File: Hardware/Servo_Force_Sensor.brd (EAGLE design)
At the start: 25.4 x 25.4 mm, 1 part

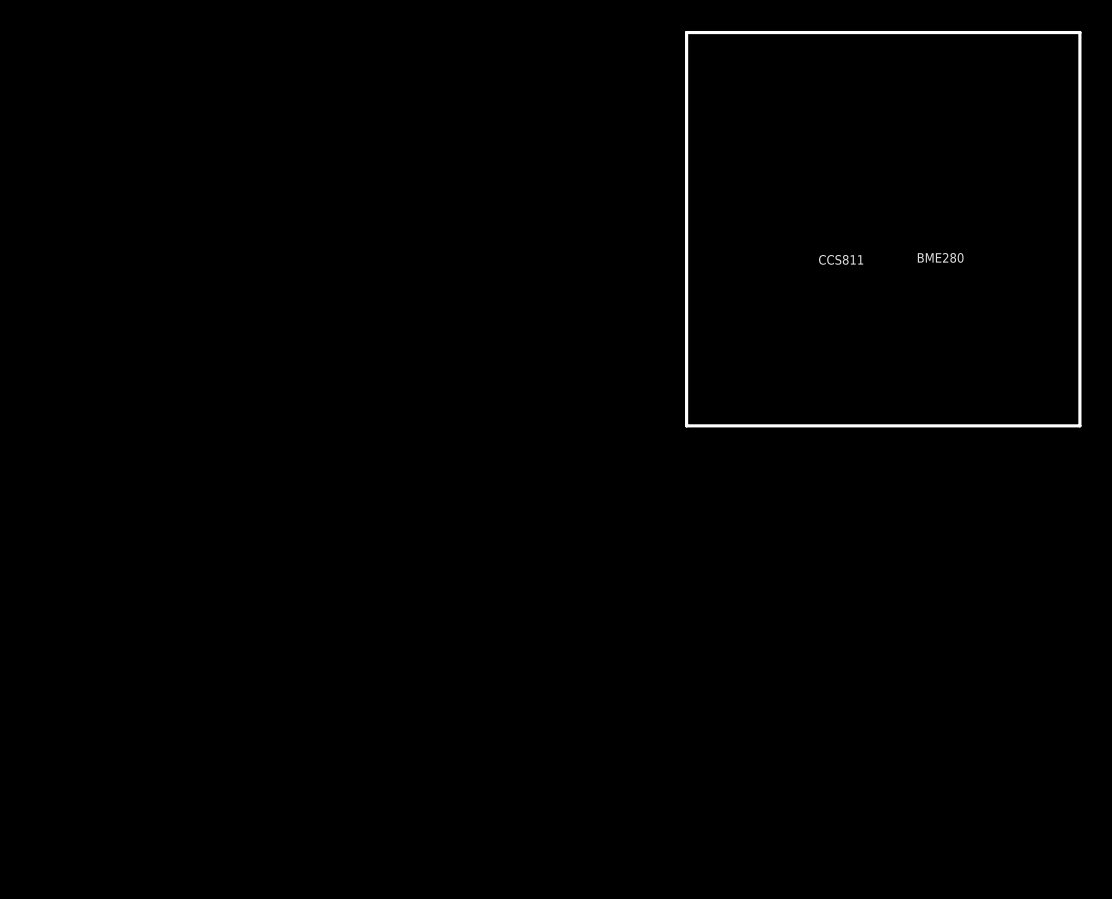
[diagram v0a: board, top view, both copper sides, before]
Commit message: library work for medium and large horns
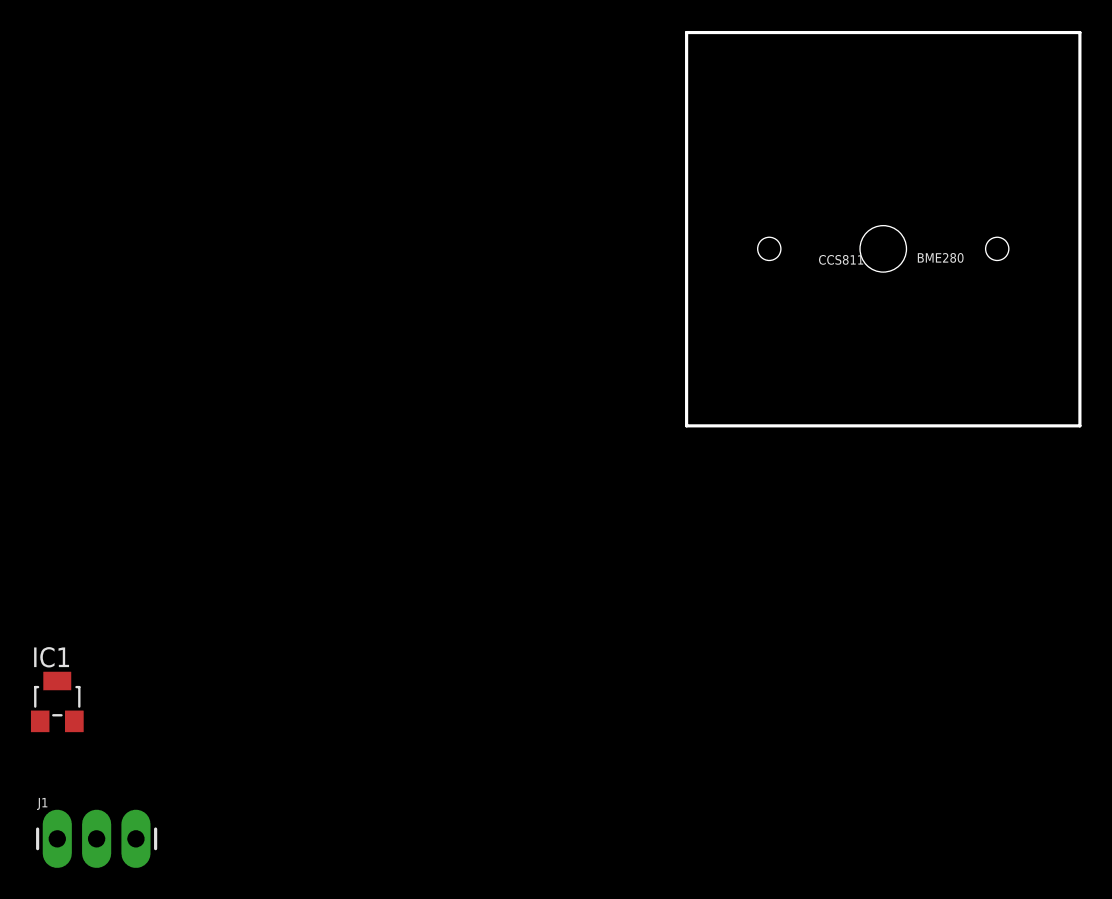
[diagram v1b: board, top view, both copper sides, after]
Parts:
- added IC1: A1302LH, allegro:SOT23-W
- added J1: (no value), SparkFun-Connectors:1X03_LONGPADS
- added U$1: (no value), Servo_Horns:MEDIUM_HORN_16MM
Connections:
- new net GND: IC1.3, J1.3
- new net OUT: IC1.2, J1.2
- new net VCC: IC1.1, J1.1
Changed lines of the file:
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@@
 <layer number="47" name="Measures" color="7" fill="1" visible="no" active="yes"/>
 <layer number="48" name="Document" color="7" fill="1" visible="no" active="yes"/>
-<layer number="49" name="Reference" color="7" fill="1" visible="no" active="yes"/>
+<layer number="49" name="Reference" color="13" fill="1" visible="yes" active="yes"/>
 <layer number="50" name="dxf" color="7" fill="1" visible="no" active="yes"/>
 <layer number="51" name="tDocu" color="6" fill="1" visible="yes" active="yes"/>
@@
 <layer number="115" name="ReferenceISLANDS" color="7" fill="1" visible="no" active="no"/>
 <layer number="116" name="Patch_BOT" color="9" fill="4" visible="no" active="no"/>
-<layer number="117" name="PM_Ref" color="26" fill="1" visible="yes" active="yes"/>
+<layer number="117" name="PM_Ref" color="26" fill="1" visible="no" active="yes"/>
 <layer number="118" name="Rect_Pads" color="7" fill="1" visible="no" active="no"/>
-<layer number="119" name="PF_Ref" color="31" fill="1" visible="yes" active="yes"/>
-<layer number="120" name="WFL_Ref" color="25" fill="1" visible="yes" active="yes"/>
+<layer number="119" name="PF_Ref" color="31" fill="1" visible="no" active="yes"/>
+<layer number="120" name="WFL_Ref" color="25" fill="1" visible="no" active="yes"/>
 <layer number="121" name="_tsilk" color="7" fill="1" visible="no" active="no"/>
 <layer number="122" name="_bsilk" color="7" fill="1" visible="no" active="no"/>
@@
 <attribute name="REV" value="" x="-13.97" y="-21.59" size="1.778" layer="27" display="off"/>
 </element>
+<element name="IC1" library="allegro" library_urn="urn:adsk.eagle:library:93" package="SOT23-W" package3d_urn="urn:adsk.eagle:package:3443/1" value="A1302LH" x="-40.64" y="-17.78" smashed="yes">
+<attribute name="MF" value="ALLEGRO MICROSYSTEMS, INC." x="-40.64" y="-17.78" size="1.778" layer="27" display="off"/>
+<attribute name="MPN" value="A1302ELHLT-T" x="-40.64" y="-17.78" size="1.778" layer="27" display="off"/>
+<attribute name="NAME" x="-42.29" y="-15.58" size="1.27" layer="25"/>
+<attribute name="OC_FARNELL" value="1457209" x="-40.64" y="-17.78" size="1.778" layer="27" display="off"/>
+<attribute name="OC_NEWARK" value="31K6638" x="-40.64" y="-17.78" size="1.778" layer="27" display="off"/>
+<attribute name="VALUE" x="-42.84" y="-21.63" size="1.27" layer="27"/>
+</element>
+<element name="J1" library="SparkFun-Connectors" package="1X03_LONGPADS" value="" x="-40.64" y="-26.67" smashed="yes">
+<attribute name="NAME" x="-41.91" y="-24.638" size="0.6096" layer="25" font="vector" ratio="20"/>
+<attribute name="VALUE" x="-41.91" y="-29.337" size="0.6096" layer="27" font="vector" ratio="20"/>
+</element>
+<element name="U$1" library="Servo_Horns" package="MEDIUM_HORN_16MM" value="" x="12.7" y="11.43" smashed="yes"/>
 </elements>
 <signals>
@@
 <vertex x="0" y="0"/>
 </polygon>
+<contactref element="IC1" pad="3"/>
+<contactref element="J1" pad="3"/>
+<wire x1="-40.64" y1="-16.48" x2="-35.56" y2="-26.67" width="0" layer="19" extent="1-1"/>
 </signal>
 <signal name="N$1">
+</signal>
+<signal name="VCC">
+<contactref element="IC1" pad="1"/>
+<contactref element="J1" pad="1"/>
+<wire x1="-41.74" y1="-19.08" x2="-40.64" y2="-26.67" width="0" layer="19" extent="1-1"/>
+</signal>
+<signal name="OUT">
+<contactref element="IC1" pad="2"/>
+<contactref element="J1" pad="2"/>
+<wire x1="-39.54" y1="-19.08" x2="-38.1" y2="-26.67" width="0" layer="19" extent="1-1"/>
 </signal>
 </signals>
@@
 </board>
 </drawing>
+<compatibility>
+<note version="8.2" severity="warning">
+Since Version 8.2, EAGLE supports online libraries. The ids
+of those online libraries will not be understood (or retained)
+with this version.
+</note>
+<note version="8.3" severity="warning">
+Since Version 8.3, EAGLE supports URNs for individual library
+assets (packages, symbols, and devices). The URNs of those assets
+will not be understood (or retained) with this version.
+</note>
+<note version="8.3" severity="warning">
+Since Version 8.3, EAGLE supports the association of 3D packages
+with devices in libraries, schematics, and board files. Those 3D
+packages will not be understood (or retained) with this version.
+</note>
+</compatibility>
 </eagle>

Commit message: finalized v01
outer shape done,
verified drill holes via lazer cut acrylic prototype
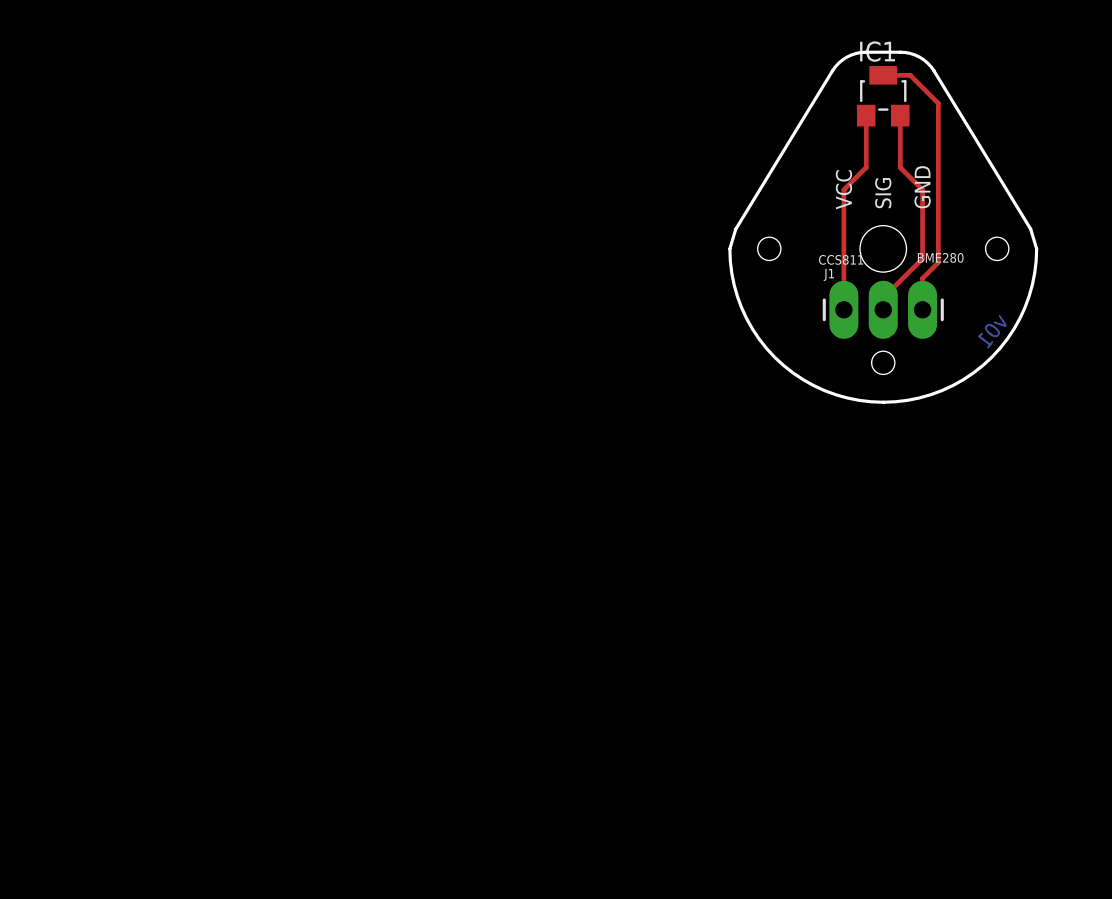
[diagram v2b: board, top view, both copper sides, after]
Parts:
- moved IC1 66.1 mm to (12.7, 21.3)
- moved J1 61.2 mm to (10.2, 7.49)
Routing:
- net GND: track 0.00 -> 18.1 mm
- net OUT: track 0.00 -> 14.2 mm
- net VCC: track 0.00 -> 13.1 mm
- removed copper zone on layer 1, net GND
- removed copper zone on layer 16, net GND
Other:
- board size 25.4 x 25.4 mm -> 19.8 x 22.6 mm
- board text added: "GND"
- board text added: "SIG"
- board text added: "VCC"
- board text added: "v01"
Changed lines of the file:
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@@
 <layer number="155" name="FabDoc3" color="7" fill="1" visible="no" active="no"/>
 <layer number="199" name="Contour" color="7" fill="1" visible="no" active="no"/>
-<layer number="200" name="200bmp" color="1" fill="10" visible="no" active="no"/>
+<layer number="200" name="200bmp" color="1" fill="10" visible="no" active="yes"/>
 <layer number="201" name="201bmp" color="2" fill="10" visible="no" active="no"/>
 <layer number="202" name="202bmp" color="3" fill="10" visible="no" active="no"/>
@@
 <board>
 <plain>
-<wire x1="0" y1="0" x2="0" y2="25.4" width="0.2032" layer="20"/>
-<wire x1="0" y1="25.4" x2="25.4" y2="25.4" width="0.2032" layer="20"/>
-<wire x1="25.4" y1="25.4" x2="25.4" y2="0" width="0.2032" layer="20"/>
-<wire x1="25.4" y1="0" x2="0" y2="0" width="0.2032" layer="20"/>
 <text x="16.51" y="-21.59" size="1.778" layer="51">Pete Lewis</text>
 <text x="8.509" y="10.414" size="0.6096" layer="25">CCS811</text>
@@
 <dimension x1="22.86" y1="22.86" x2="0" y2="22.86" x3="11.43" y3="30.48" textsize="1.778" layer="47"/>
 <text x="-1.27" y="-12.7" size="1.778" layer="47">Measurements in mm</text>
+<wire x1="22.225" y1="12.7" x2="15.982815625" y2="22.914484375" width="0.2032" layer="20"/>
+<wire x1="15.982815625" y1="22.914484375" x2="13.81548125" y2="24.13" width="0.2032" layer="20" curve="58.570451"/>
+<wire x1="13.81548125" y1="24.13" x2="11.58451875" y2="24.13" width="0.2032" layer="20"/>
+<wire x1="11.58451875" y1="24.13" x2="9.417184375" y2="22.914484375" width="0.2032" layer="20" curve="58.570391"/>
+<wire x1="9.417184375" y1="22.914484375" x2="3.175" y2="12.7" width="0.2032" layer="20"/>
+<wire x1="3.175" y1="12.7" x2="2.794" y2="11.43" width="0.2032" layer="20"/>
+<wire x1="22.606" y1="11.43" x2="22.225" y2="12.7" width="0.2032" layer="20"/>
+<text x="15.24" y="13.97" size="1.016" layer="21" font="vector" ratio="15" rot="R90" align="center-left">GND</text>
+<text x="10.16" y="13.97" size="1.016" layer="21" font="vector" ratio="15" rot="R90" align="center-left">VCC</text>
+<wire x1="2.794" y1="11.43" x2="12.7" y2="1.524" width="0.2032" layer="20" curve="90"/>
+<wire x1="12.7" y1="1.524" x2="22.606" y2="11.43" width="0.2032" layer="20" curve="90"/>
+<text x="12.7" y="13.97" size="1.016" layer="21" font="vector" ratio="15" rot="R90" align="center-left">SIG</text>
+<text x="19.016790625" y="5.208446875" size="1.016" layer="16" font="vector" ratio="20" rot="MR128" align="center-left">v01</text>
 </plain>
 <attributes>
@@
 <attribute name="REV" value="" x="-13.97" y="-21.59" size="1.778" layer="27" display="off"/>
 </element>
-<element name="IC1" library="allegro" library_urn="urn:adsk.eagle:library:93" package="SOT23-W" package3d_urn="urn:adsk.eagle:package:3443/1" value="A1302LH" x="-40.64" y="-17.78" smashed="yes">
-<attribute name="MF" value="ALLEGRO MICROSYSTEMS, INC." x="-40.64" y="-17.78" size="1.778" layer="27" display="off"/>
-<attribute name="MPN" value="A1302ELHLT-T" x="-40.64" y="-17.78" size="1.778" layer="27" display="off"/>
-<attribute name="NAME" x="-42.29" y="-15.58" size="1.27" layer="25"/>
-<attribute name="OC_FARNELL" value="1457209" x="-40.64" y="-17.78" size="1.778" layer="27" display="off"/>
-<attribute name="OC_NEWARK" value="31K6638" x="-40.64" y="-17.78" size="1.778" layer="27" display="off"/>
-<attribute name="VALUE" x="-42.84" y="-21.63" size="1.27" layer="27"/>
+<element name="IC1" library="allegro" library_urn="urn:adsk.eagle:library:93" package="SOT23-W" package3d_urn="urn:adsk.eagle:package:3443/1" value="A1302LH" x="12.7" y="21.336" smashed="yes">
+<attribute name="MF" value="ALLEGRO MICROSYSTEMS, INC." x="12.7" y="21.336" size="1.778" layer="27" display="off"/>
+<attribute name="MPN" value="A1302ELHLT-T" x="12.7" y="21.336" size="1.778" layer="27" display="off"/>
+<attribute name="NAME" x="11.05" y="23.536" size="1.27" layer="25"/>
+<attribute name="OC_FARNELL" value="1457209" x="12.7" y="21.336" size="1.778" layer="27" display="off"/>
+<attribute name="OC_NEWARK" value="31K6638" x="12.7" y="21.336" size="1.778" layer="27" display="off"/>
+<attribute name="VALUE" x="10.5" y="17.486" size="1.27" layer="27"/>
 </element>
-<element name="J1" library="SparkFun-Connectors" package="1X03_LONGPADS" value="" x="-40.64" y="-26.67" smashed="yes">
-<attribute name="NAME" x="-41.91" y="-24.638" size="0.6096" layer="25" font="vector" ratio="20"/>
-<attribute name="VALUE" x="-41.91" y="-29.337" size="0.6096" layer="27" font="vector" ratio="20"/>
+<element name="J1" library="SparkFun-Connectors" package="1X03_LONGPADS" value="" x="10.16" y="7.493" smashed="yes">
+<attribute name="NAME" x="8.89" y="9.525" size="0.6096" layer="25" font="vector" ratio="20"/>
+<attribute name="VALUE" x="8.89" y="4.826" size="0.6096" layer="27" font="vector" ratio="20"/>
 </element>
 <element name="U$1" library="Servo_Horns" package="MEDIUM_HORN_16MM" value="" x="12.7" y="11.43" smashed="yes"/>
@@
 <signals>
 <signal name="GND">
-<polygon width="0.2032" layer="1" isolate="0.3048">
-<vertex x="0" y="0"/>
-<vertex x="25.4" y="0"/>
-<vertex x="25.4" y="25.4"/>
-<vertex x="0" y="25.4"/>
-</polygon>
-<polygon width="0.2032" layer="16" isolate="0.3048">
-<vertex x="0" y="25.4"/>
-<vertex x="25.4" y="25.4"/>
-<vertex x="25.4" y="0"/>
-<vertex x="0" y="0"/>
-</polygon>
 <contactref element="IC1" pad="3"/>
 <contactref element="J1" pad="3"/>
-<wire x1="-40.64" y1="-16.48" x2="-35.56" y2="-26.67" width="0" layer="19" extent="1-1"/>
+<wire x1="15.24" y1="7.493" x2="15.24" y2="9.525" width="0.3048" layer="1"/>
+<wire x1="15.24" y1="9.525" x2="16.256" y2="10.541" width="0.3048" layer="1"/>
+<wire x1="16.256" y1="10.541" x2="16.256" y2="20.828" width="0.3048" layer="1"/>
+<wire x1="14.448" y1="22.636" x2="12.7" y2="22.636" width="0.3048" layer="1"/>
+<wire x1="16.256" y1="20.828" x2="14.448" y2="22.636" width="0.3048" layer="1"/>
 </signal>
 <signal name="N$1">
@@
 <contactref element="IC1" pad="1"/>
 <contactref element="J1" pad="1"/>
-<wire x1="-41.74" y1="-19.08" x2="-40.64" y2="-26.67" width="0" layer="19" extent="1-1"/>
+<wire x1="11.6" y1="20.036" x2="11.6" y2="16.68" width="0.3048" layer="1"/>
+<wire x1="11.6" y1="16.68" x2="10.16" y2="15.24" width="0.3048" layer="1"/>
+<wire x1="10.16" y1="15.24" x2="10.16" y2="7.493" width="0.3048" layer="1"/>
 </signal>
 <signal name="OUT">
 <contactref element="IC1" pad="2"/>
 <contactref element="J1" pad="2"/>
-<wire x1="-39.54" y1="-19.08" x2="-38.1" y2="-26.67" width="0" layer="19" extent="1-1"/>
+<wire x1="13.8" y1="20.036" x2="13.8" y2="16.68" width="0.3048" layer="1"/>
+<wire x1="13.8" y1="16.68" x2="15.24" y2="15.24" width="0.3048" layer="1"/>
+<wire x1="15.24" y1="10.795" x2="12.7" y2="8.255" width="0.3048" layer="1"/>
+<wire x1="12.7" y1="8.255" x2="12.7" y2="7.493" width="0.3048" layer="1"/>
+<wire x1="15.24" y1="15.24" x2="15.24" y2="10.795" width="0.3048" layer="1"/>
 </signal>
 </signals>
